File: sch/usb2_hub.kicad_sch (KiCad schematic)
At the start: 40 parts

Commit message: annotated components
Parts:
- U5, U6: renamed from U?; LCSC (none) -> C144190
- U7: renamed from U?; LCSC (none) -> C58940
- gave numbers to parts that had none: 37

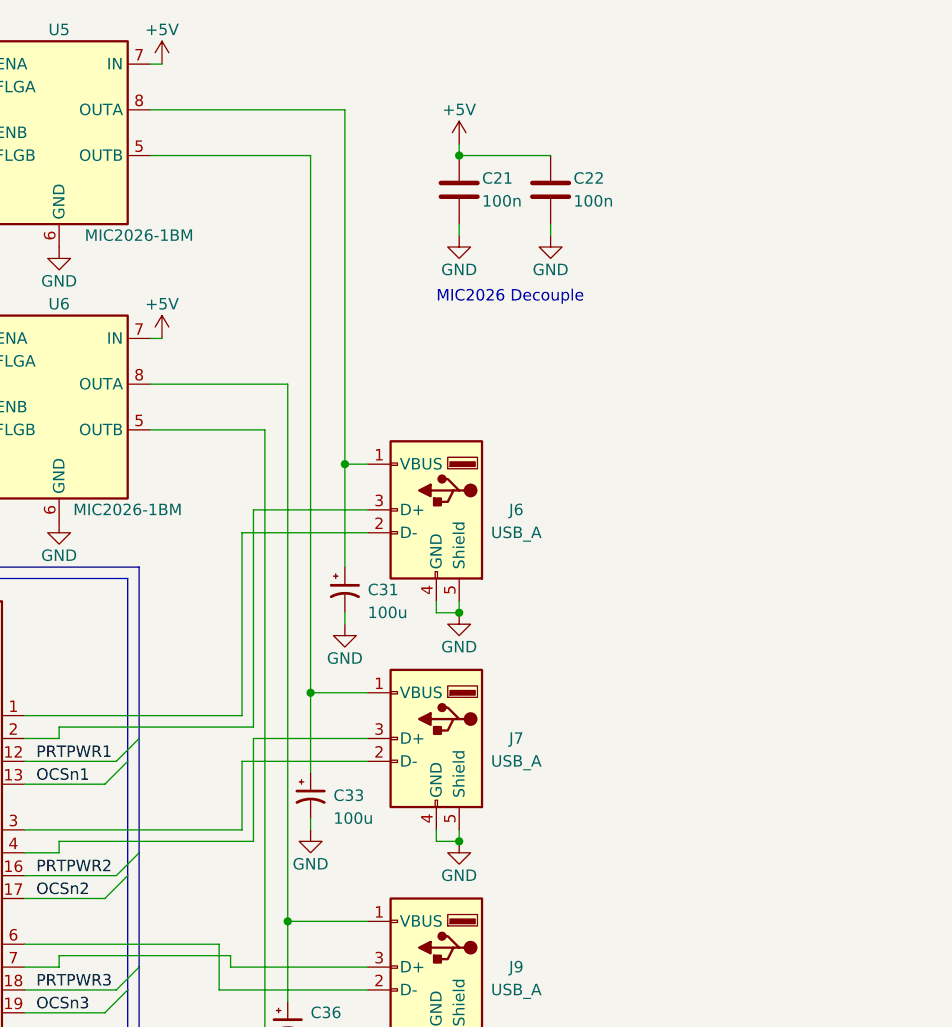
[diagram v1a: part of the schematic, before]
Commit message: updated power on leds, hub 4 LEDs and misc
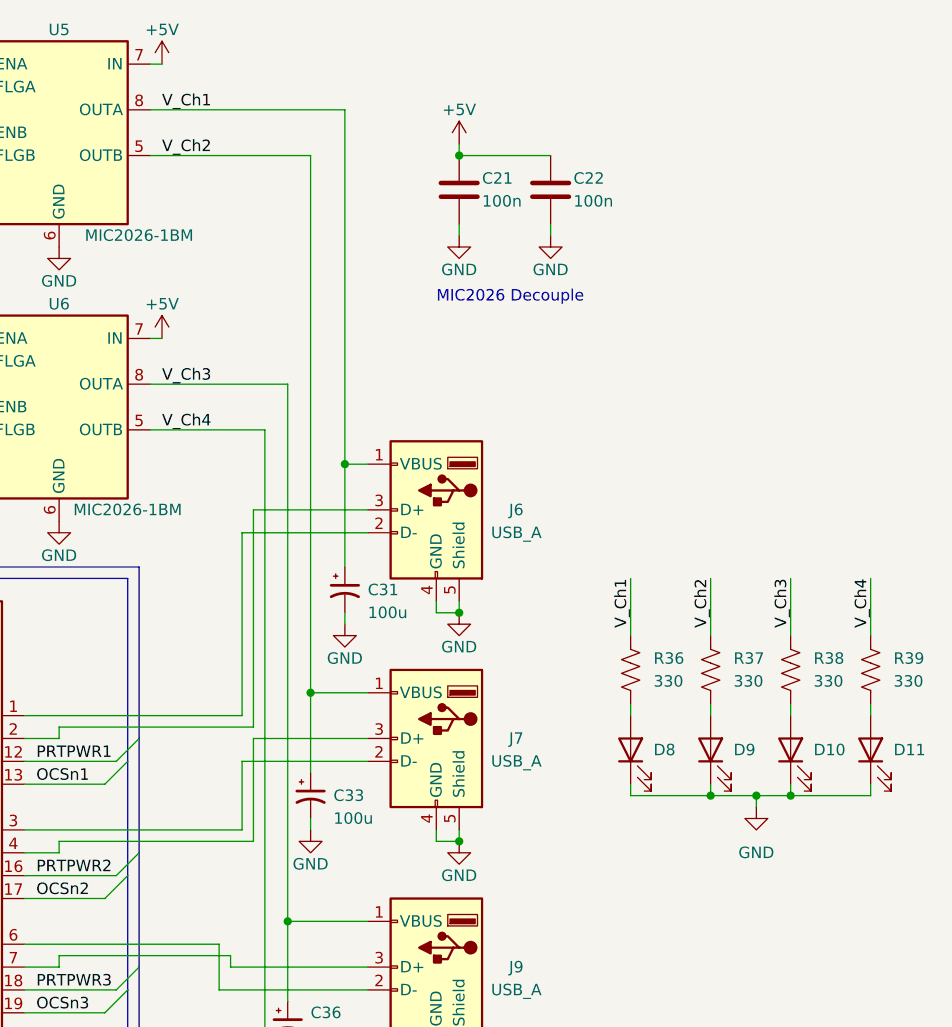
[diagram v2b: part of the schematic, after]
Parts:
- added D10, D11, D8, D9: 19-217/GHC-YR1S2/3T, Diode_SMD:D_0603_1608Metric_Pad1.05x0.95mm_HandSolder, symbol Device:LED
- added R36, R37, R38, R39: 330, Resistor_SMD:R_0402_1005Metric_Pad0.72x0.64mm_HandSolder, symbol Device:R_US
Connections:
- net GND: now also D10.1 (K), D11.1 (K), D8.1 (K), D9.1 (K)
- net V_Ch1: now reaches C31.1, J6.1 (VBUS), U5.8 (OUTA)
- net V_Ch1: now also R36.1
- net V_Ch4: now reaches C40.1, J10.1 (VBUS), U6.5 (OUTB)
- net V_Ch4: now also R39.1
- net V_Ch3: now reaches C36.1, J9.1 (VBUS), U6.8 (OUTA)
- net V_Ch3: now also R38.1
- net V_Ch2: now reaches C33.1, J7.1 (VBUS), U5.5 (OUTB)
- net V_Ch2: now also R37.1
- new net: D11.2 (A), R39.2
- new net: D10.2 (A), R38.2
- new net: D9.2 (A), R37.2
- new net: D8.2 (A), R36.2

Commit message: updated 3d models, broken footprints, pcb re-import
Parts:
- R22: footprint (none) -> Resistor_SMD:R_0603_1608Metric_Pad0.98x0.95mm_HandSolder
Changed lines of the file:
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@@
     (property "Reference" "R22" (id 0) (at 113.03 109.22 90))
     (property "Value" "12K" (id 1) (at 113.03 111.76 90))
-    (property "Footprint" "" (id 2) (at 113.03 116.078 90)
+    (property "Footprint" "Resistor_SMD:R_0603_1608Metric_Pad0.98x0.95mm_HandSolder" (id 2) (at 113.03 116.078 90)
       (effects (font (size 1.27 1.27)) hide)
     )

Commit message: fix sch unexpect to gnd; usb to right angle; pcb boarder increased to pi size
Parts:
- J10, J9: footprint Connector_USB:USB_A_CONNFLY_DS1095-WNR0 -> Connector_USB:USB_A_Wuerth_614004134726_Horizontal; LCSC C2346 -> C720524
- J6, J7: footprint Connector_USB:USB_A_CONNFLY_DS1095-WNR0 -> Connector_USB:USB_A_Wuerth_61400826021_Horizontal_Stacked; LCSC C2346 -> C720524
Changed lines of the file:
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@@
     (property "Reference" "J9" (id 0) (at 233.68 121.92 0))
     (property "Value" "USB_A" (id 1) (at 233.68 124.46 0))
-    (property "Footprint" "Connector_USB:USB_A_CONNFLY_DS1095-WNR0" (id 2) (at 220.98 123.19 0)
+    (property "Footprint" "Connector_USB:USB_A_Wuerth_614004134726_Horizontal" (id 2) (at 220.98 123.19 0)
       (effects (font (size 1.27 1.27)) hide)
     )
@@
       (effects (font (size 1.27 1.27)) hide)
     )
-    (property "LCSC" "C2346" (id 4) (at 224.79 121.92 0)
+    (property "LCSC" "C720524" (id 4) (at 224.79 121.92 0)
       (effects (font (size 1.27 1.27)) hide)
     )
@@
     (property "Reference" "J7" (id 0) (at 233.68 96.52 0))
     (property "Value" "USB_A" (id 1) (at 233.68 99.06 0))
-    (property "Footprint" "Connector_USB:USB_A_CONNFLY_DS1095-WNR0" (id 2) (at 220.98 97.79 0)
+    (property "Footprint" "Connector_USB:USB_A_Wuerth_61400826021_Horizontal_Stacked" (id 2) (at 220.98 97.79 0)
       (effects (font (size 1.27 1.27)) hide)
     )
@@
       (effects (font (size 1.27 1.27)) hide)
     )
-    (property "LCSC" "C2346" (id 4) (at 224.79 96.52 0)
+    (property "LCSC" "C720524" (id 4) (at 224.79 96.52 0)
       (effects (font (size 1.27 1.27)) hide)
     )
@@
     (property "Reference" "J6" (id 0) (at 233.68 71.12 0))
     (property "Value" "USB_A" (id 1) (at 233.68 73.66 0))
-    (property "Footprint" "Connector_USB:USB_A_CONNFLY_DS1095-WNR0" (id 2) (at 220.98 72.39 0)
+    (property "Footprint" "Connector_USB:USB_A_Wuerth_61400826021_Horizontal_Stacked" (id 2) (at 220.98 72.39 0)
       (effects (font (size 1.27 1.27)) hide)
     )
@@
       (effects (font (size 1.27 1.27)) hide)
     )
-    (property "LCSC" "C2346" (id 4) (at 224.79 71.12 0)
+    (property "LCSC" "C720524" (id 4) (at 224.79 71.12 0)
       (effects (font (size 1.27 1.27)) hide)
     )
@@
     (property "Reference" "J10" (id 0) (at 233.68 148.59 0))
     (property "Value" "USB_A" (id 1) (at 233.68 151.13 0))
-    (property "Footprint" "Connector_USB:USB_A_CONNFLY_DS1095-WNR0" (id 2) (at 220.98 149.86 0)
+    (property "Footprint" "Connector_USB:USB_A_Wuerth_614004134726_Horizontal" (id 2) (at 220.98 149.86 0)
       (effects (font (size 1.27 1.27)) hide)
     )
@@
       (effects (font (size 1.27 1.27)) hide)
     )
-    (property "LCSC" "C2346" (id 4) (at 224.79 148.59 0)
-      (effects (font (size 1.27 1.27)) hide)
-    )
+    (property "LCSC" "C720524" (id 4) (at 224.79 148.59 0)
+      (effects (font (size 1.27 1.27)) hide)
+    )

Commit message: updated sch RESET pin ctrl
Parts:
- added Q2: 2N7002P, Package_TO_SOT_SMD:SOT-23, symbol Transistor_FET:2N7002
- C34: value 100n -> DNP; LCSC C1525 -> (none)
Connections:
- net GND: now also Q2.2 (S)
- net RESETn: now also Q2.3 (D)
- net at J8.2 (D-): now also U7.30 (USBDM_UP); no longer U7.31 (USBDP_UP)
- net at J8.3 (D+): now also U7.31 (USBDP_UP); no longer U7.30 (USBDM_UP)
- new net RST: Q2.1 (G)
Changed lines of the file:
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@@
   (junction (at 88.9 72.39) (diameter 0) (color 0 0 0 0)
   )
+  (junction (at 46.99 125.73) (diameter 0) (color 0 0 0 0)
+  )
   (junction (at 227.33 82.55) (diameter 0) (color 0 0 0 0)
   )
@@
     (stroke (width 0) (type default) (color 0 0 0 0))
   )
+  (wire (pts (xy 99.06 99.06) (xy 99.06 102.87))
+    (stroke (width 0) (type default) (color 0 0 0 0))
+  )
   (wire (pts (xy 143.51 76.2) (xy 143.51 64.77))
     (stroke (width 0) (type default) (color 0 0 0 0))
@@
     (stroke (width 0) (type default) (color 0 0 0 0))
   )
-  (wire (pts (xy 38.1 43.18) (xy 43.18 43.18))
+  (wire (pts (xy 34.29 43.18) (xy 43.18 43.18))
     (stroke (width 0) (type default) (color 0 0 0 0))
   )
@@
     (stroke (width 0) (type default) (color 0 0 0 0))
   )
-  (wire (pts (xy 83.82 99.06) (xy 123.19 99.06))
+  (wire (pts (xy 99.06 102.87) (xy 93.98 102.87))
     (stroke (width 0) (type default) (color 0 0 0 0))
   )
@@
     (stroke (width 0) (type default) (color 0 0 0 0))
   )
-  (wire (pts (xy 38.1 40.64) (xy 43.18 40.64))
+  (wire (pts (xy 34.29 40.64) (xy 43.18 40.64))
     (stroke (width 0) (type default) (color 0 0 0 0))
   )
@@
     (stroke (width 0) (type default) (color 0 0 0 0))
   )
+  (wire (pts (xy 96.52 101.6) (xy 96.52 99.06))
+    (stroke (width 0) (type default) (color 0 0 0 0))
+  )
   (wire (pts (xy 214.63 66.04) (xy 217.17 66.04))
     (stroke (width 0) (type default) (color 0 0 0 0))
@@
     (stroke (width 0) (type default) (color 0 0 0 0))
   )
+  (wire (pts (xy 93.98 102.87) (xy 93.98 101.6))
+    (stroke (width 0) (type default) (color 0 0 0 0))
+  )
   (wire (pts (xy 210.82 91.44) (xy 210.82 100.33))
     (stroke (width 0) (type default) (color 0 0 0 0))
@@
     (stroke (width 0) (type default) (color 0 0 0 0))
   )
+  (wire (pts (xy 93.98 101.6) (xy 83.82 101.6))
+    (stroke (width 0) (type default) (color 0 0 0 0))
+  )
   (wire (pts (xy 154.94 43.18) (xy 154.94 76.2))
     (stroke (width 0) (type default) (color 0 0 0 0))
@@
     (stroke (width 0) (type default) (color 0 0 0 0))
   )
-  (wire (pts (xy 38.1 45.72) (xy 43.18 45.72))
+  (wire (pts (xy 38.1 48.26) (xy 43.18 48.26))
     (stroke (width 0) (type default) (color 0 0 0 0))
   )
@@
     (stroke (width 0) (type default) (color 0 0 0 0))
   )
-  (wire (pts (xy 83.82 101.6) (xy 123.19 101.6))
-    (stroke (width 0) (type default) (color 0 0 0 0))
-  )
   (bus (pts (xy 162.56 64.77) (xy 162.56 78.74))
     (stroke (width 0) (type default) (color 0 0 0 0))
@@
     (stroke (width 0) (type default) (color 0 0 0 0))
   )
+  (wire (pts (xy 22.86 120.65) (xy 31.75 120.65))
+    (stroke (width 0) (type default) (color 0 0 0 0))
+  )
   (wire (pts (xy 179.07 124.46) (xy 189.23 124.46))
     (stroke (width 0) (type default) (color 0 0 0 0))
@@
     (stroke (width 0) (type default) (color 0 0 0 0))
   )
+  (wire (pts (xy 39.37 115.57) (xy 46.99 115.57))
+    (stroke (width 0) (type default) (color 0 0 0 0))
+  )
   (wire (pts (xy 237.49 39.37) (xy 237.49 40.64))
     (stroke (width 0) (type default) (color 0 0 0 0))
@@
     (stroke (width 0) (type default) (color 0 0 0 0))
   )
+  (wire (pts (xy 39.37 125.73) (xy 46.99 125.73))
+    (stroke (width 0) (type default) (color 0 0 0 0))
+  )
   (wire (pts (xy 260.35 102.87) (xy 260.35 104.14))
     (stroke (width 0) (type default) (color 0 0 0 0))
@@
     (stroke (width 0) (type default) (color 0 0 0 0))
   )
+  (wire (pts (xy 96.52 99.06) (xy 83.82 99.06))
+    (stroke (width 0) (type default) (color 0 0 0 0))
+  )
   (wire (pts (xy 205.74 143.51) (xy 205.74 152.4))
     (stroke (width 0) (type default) (color 0 0 0 0))
@@
     (stroke (width 0) (type default) (color 0 0 0 0))
   )
+  (wire (pts (xy 34.29 45.72) (xy 43.18 45.72))
+    (stroke (width 0) (type default) (color 0 0 0 0))
+  )
   (wire (pts (xy 204.47 96.52) (xy 204.47 107.95))
     (stroke (width 0) (type default) (color 0 0 0 0))
@@
     (stroke (width 0) (type default) (color 0 0 0 0))
   )
+  (wire (pts (xy 123.19 99.06) (xy 99.06 99.06))
+    (stroke (width 0) (type default) (color 0 0 0 0))
+  )
   (wire (pts (xy 205.74 157.48) (xy 205.74 158.75))
     (stroke (width 0) (type default) (color 0 0 0 0))
@@
   )
   (wire (pts (xy 264.16 102.87) (xy 273.05 102.87))
+    (stroke (width 0) (type default) (color 0 0 0 0))
+  )
+  (wire (pts (xy 123.19 101.6) (xy 96.52 101.6))
     (stroke (width 0) (type default) (color 0 0 0 0))
   )
@@
     (effects (font (size 1.27 1.27)) (justify left bottom))
   )
-  (label "SDA" (at 38.1 43.18 0)
+  (label "SDA" (at 34.29 43.18 0)
     (effects (font (size 1.27 1.27)) (justify left bottom))
   )
@@
     (effects (font (size 1.27 1.27)) (justify left bottom))
   )
-  (label "SCL" (at 38.1 40.64 0)
+  (label "SCL" (at 34.29 40.64 0)
     (effects (font (size 1.27 1.27)) (justify left bottom))
   )
@@
     (effects (font (size 1.27 1.27)) (justify left bottom))
   )
+  (label "RST_CTL" (at 34.29 45.72 0)
+    (effects (font (size 1.27 1.27)) (justify left bottom))
+  )
   (label "PRTPWR2" (at 163.83 29.21 0)
     (effects (font (size 1.27 1.27)) (justify left bottom))
@@
   )
   (label "SCL" (at 118.11 137.16 0)
+    (effects (font (size 1.27 1.27)) (justify left bottom))
+  )
+  (label "RST_CTL" (at 22.86 120.65 0)
     (effects (font (size 1.27 1.27)) (justify left bottom))
   )
@@
     (effects (font (size 1.27 1.27)) (justify left))
   )
-  (hierarchical_label "GND" (shape input) (at 43.18 45.72 0)
+  (hierarchical_label "RST" (shape input) (at 43.18 45.72 0)
+    (effects (font (size 1.27 1.27)) (justify left))
+  )
+  (hierarchical_label "GND" (shape input) (at 43.18 48.26 0)
     (effects (font (size 1.27 1.27)) (justify left))
   )
@@
       (effects (font (size 1.27 1.27)) (justify left))
     )
-    (property "Value" "100n" (id 1) (at 49.53 121.92 0)
+    (property "Value" "DNP" (id 1) (at 49.53 121.92 0)
       (effects (font (size 1.27 1.27)) (justify left))
     )
@@
     )
     (property "Datasheet" "~" (id 3) (at 46.99 120.65 0)
-      (effects (font (size 1.27 1.27)) hide)
-    )
-    (property "LCSC" "C1525" (id 4) (at 46.99 120.65 0)
       (effects (font (size 1.27 1.27)) hide)
     )
@@
     (pin "2")
   )
-  (symbol (lib_id "power:GND") (at 38.1 45.72 0) (unit 1)
+  (symbol (lib_id "power:GND") (at 38.1 48.26 0) (unit 1)
     (in_bom yes) (on_board yes) (fields_autoplaced)
-    (property "Reference" "#PWR070" (id 0) (at 38.1 52.07 0)
-      (effects (font (size 1.27 1.27)) hide)
-    )
-    (property "Value" "GND" (id 1) (at 38.1 50.8 0))
-    (property "Footprint" "" (id 2) (at 38.1 45.72 0)
-      (effects (font (size 1.27 1.27)) hide)
-    )
-    (property "Datasheet" "" (id 3) (at 38.1 45.72 0)
+    (property "Reference" "#PWR070" (id 0) (at 38.1 54.61 0)
+      (effects (font (size 1.27 1.27)) hide)
+    )
+    (property "Value" "GND" (id 1) (at 38.1 53.34 0))
+    (property "Footprint" "" (id 2) (at 38.1 48.26 0)
+      (effects (font (size 1.27 1.27)) hide)
+    )
+    (property "Datasheet" "" (id 3) (at 38.1 48.26 0)
       (effects (font (size 1.27 1.27)) hide)
     )
@@
     (pin "2")
   )
+  (symbol (lib_id "Transistor_FET:2N7002") (at 36.83 120.65 0) (unit 1)
+    (in_bom yes) (on_board yes)
+    (property "Reference" "Q2" (id 0) (at 41.91 119.38 0)
+      (effects (font (size 1.27 1.27)) (justify left))
+    )
+    (property "Value" "2N7002P" (id 1) (at 27.94 124.46 0)
+      (effects (font (size 1.27 1.27)) (justify left))
+    )
+    (property "Footprint" "Package_TO_SOT_SMD:SOT-23" (id 2) (at 41.91 122.555 0)
+      (effects (font (size 1.27 1.27) italic) (justify left) hide)
+    )
+    (property "Datasheet" "https://www.onsemi.com/pub/Collateral/NDS7002A-D.PDF" (id 3) (at 36.83 120.65 0)
+      (effects (font (size 1.27 1.27)) (justify left) hide)
+    )
+    (property "LCSC" "C8545" (id 4) (at 36.83 120.65 0)
+      (effects (font (size 1.27 1.27)) hide)
+    )
+    (pin "1")
+    (pin "2")
+    (pin "3")
+  )
   (symbol (lib_id "Device:C") (at 110.49 133.35 0) (unit 1)

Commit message: correct usb footprints
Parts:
- J6, J7: footprint Connector_USB:USB_A_Wuerth_61400826021_Horizontal_Stacked -> Connector_USB:USB_A_Wuerth_614004134726_Horizontal
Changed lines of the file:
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@@
     (property "Reference" "J7" (id 0) (at 233.68 96.52 0))
     (property "Value" "USB_A" (id 1) (at 233.68 99.06 0))
-    (property "Footprint" "Connector_USB:USB_A_Wuerth_61400826021_Horizontal_Stacked" (id 2) (at 220.98 97.79 0)
+    (property "Footprint" "Connector_USB:USB_A_Wuerth_614004134726_Horizontal" (id 2) (at 220.98 97.79 0)
       (effects (font (size 1.27 1.27)) hide)
     )
@@
     (property "Reference" "J6" (id 0) (at 233.68 71.12 0))
     (property "Value" "USB_A" (id 1) (at 233.68 73.66 0))
-    (property "Footprint" "Connector_USB:USB_A_Wuerth_61400826021_Horizontal_Stacked" (id 2) (at 220.98 72.39 0)
+    (property "Footprint" "Connector_USB:USB_A_Wuerth_614004134726_Horizontal" (id 2) (at 220.98 72.39 0)
       (effects (font (size 1.27 1.27)) hide)
     )
